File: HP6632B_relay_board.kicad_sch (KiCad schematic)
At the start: 23 parts, among them J1 Molex 26-60-4090 (KK396), J610 68610814422 8 pos 1mm FFC, J620 Molex 09-48-1094 or 09-48-3095, K601 V23105-A5303-A201, K602 V23105-A5303-A201, K603 V23105-A5303-A201, K604 ST2-DC12V-F, K605 ST2-DC12V-F, U601 NCV1413B

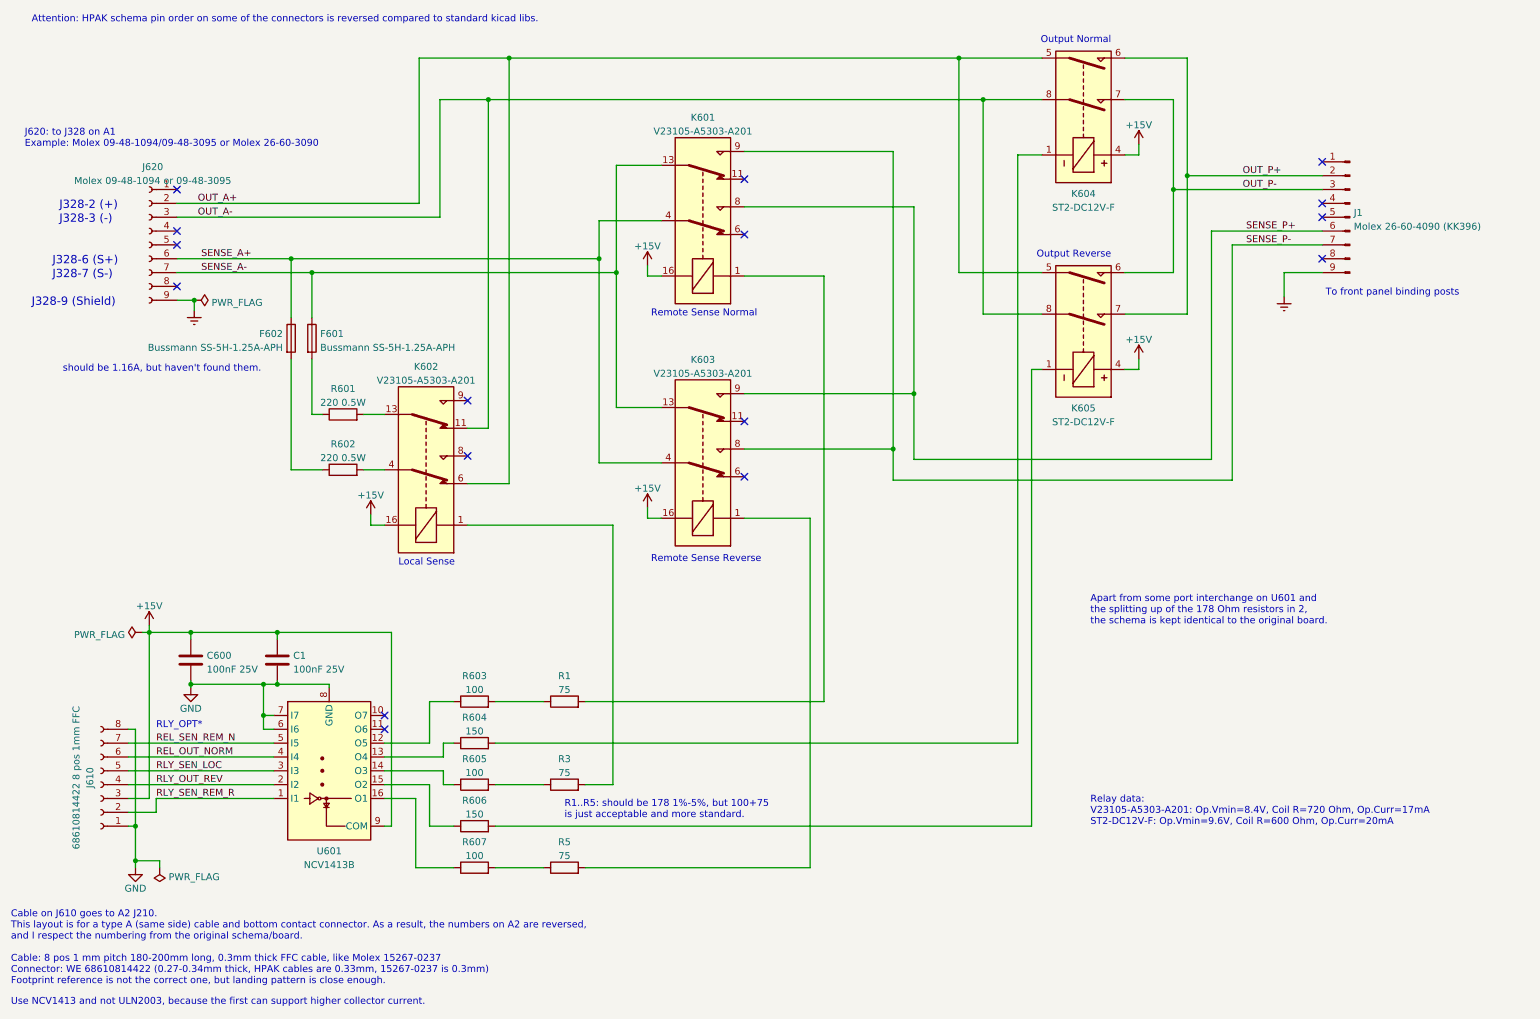
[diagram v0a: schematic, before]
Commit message: update to newer kicad version, added interactive BOM
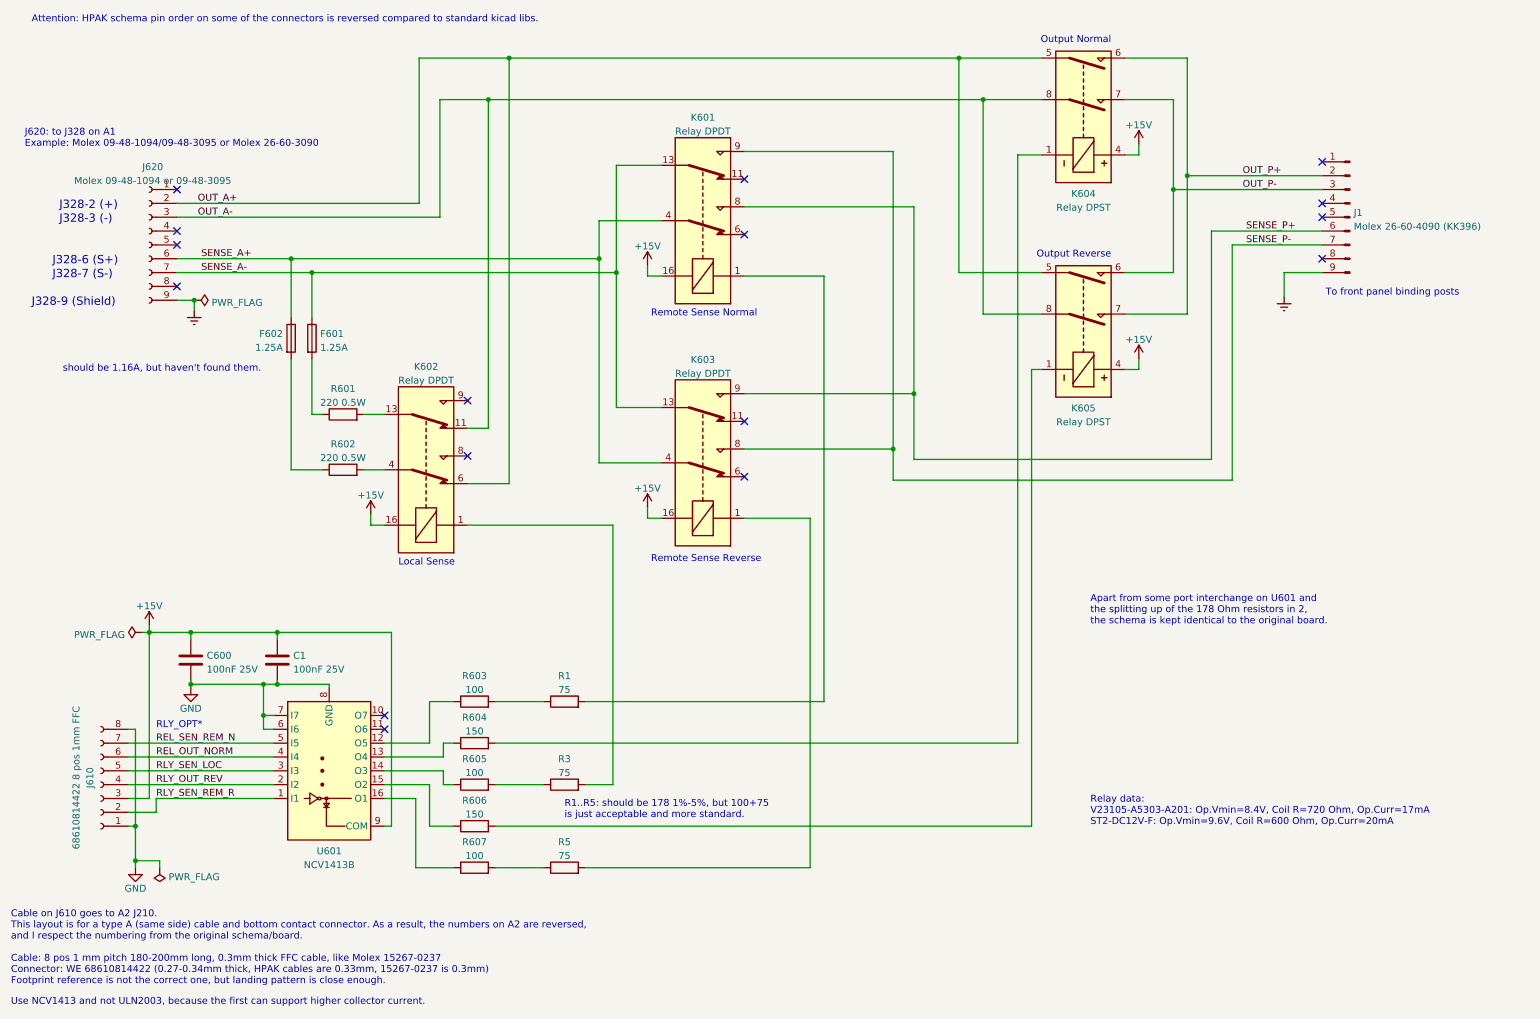
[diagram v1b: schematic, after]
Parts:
- F601, F602: value Bussmann SS-5H-1.25A-APH -> 1.25A; MFN (none) -> Bussmann; PN (none) -> SS-5H-1.25A-APH
- J1: MFN (none) -> Molex; PN (none) -> 26-60-4090 (KK396)
- J610: MFN (none) -> Wurth; PN (none) -> 68610814422
- J620: MFN (none) -> Molex; PN (none) -> 09-48-1094 or 09-48-3095
- K601, K602, K603: value V23105-A5303-A201 -> Relay DPDT; MFN (none) -> TE; PN (none) -> V23105-A5303-A201
- K604, K605: value ST2-DC12V-F -> Relay DPST; MFN (none) -> Panasonic; PN (none) -> ST2-DC12V-F
- U601: PN (none) -> NCV1413B
